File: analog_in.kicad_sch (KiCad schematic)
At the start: 5 parts, among them U18 INA600B

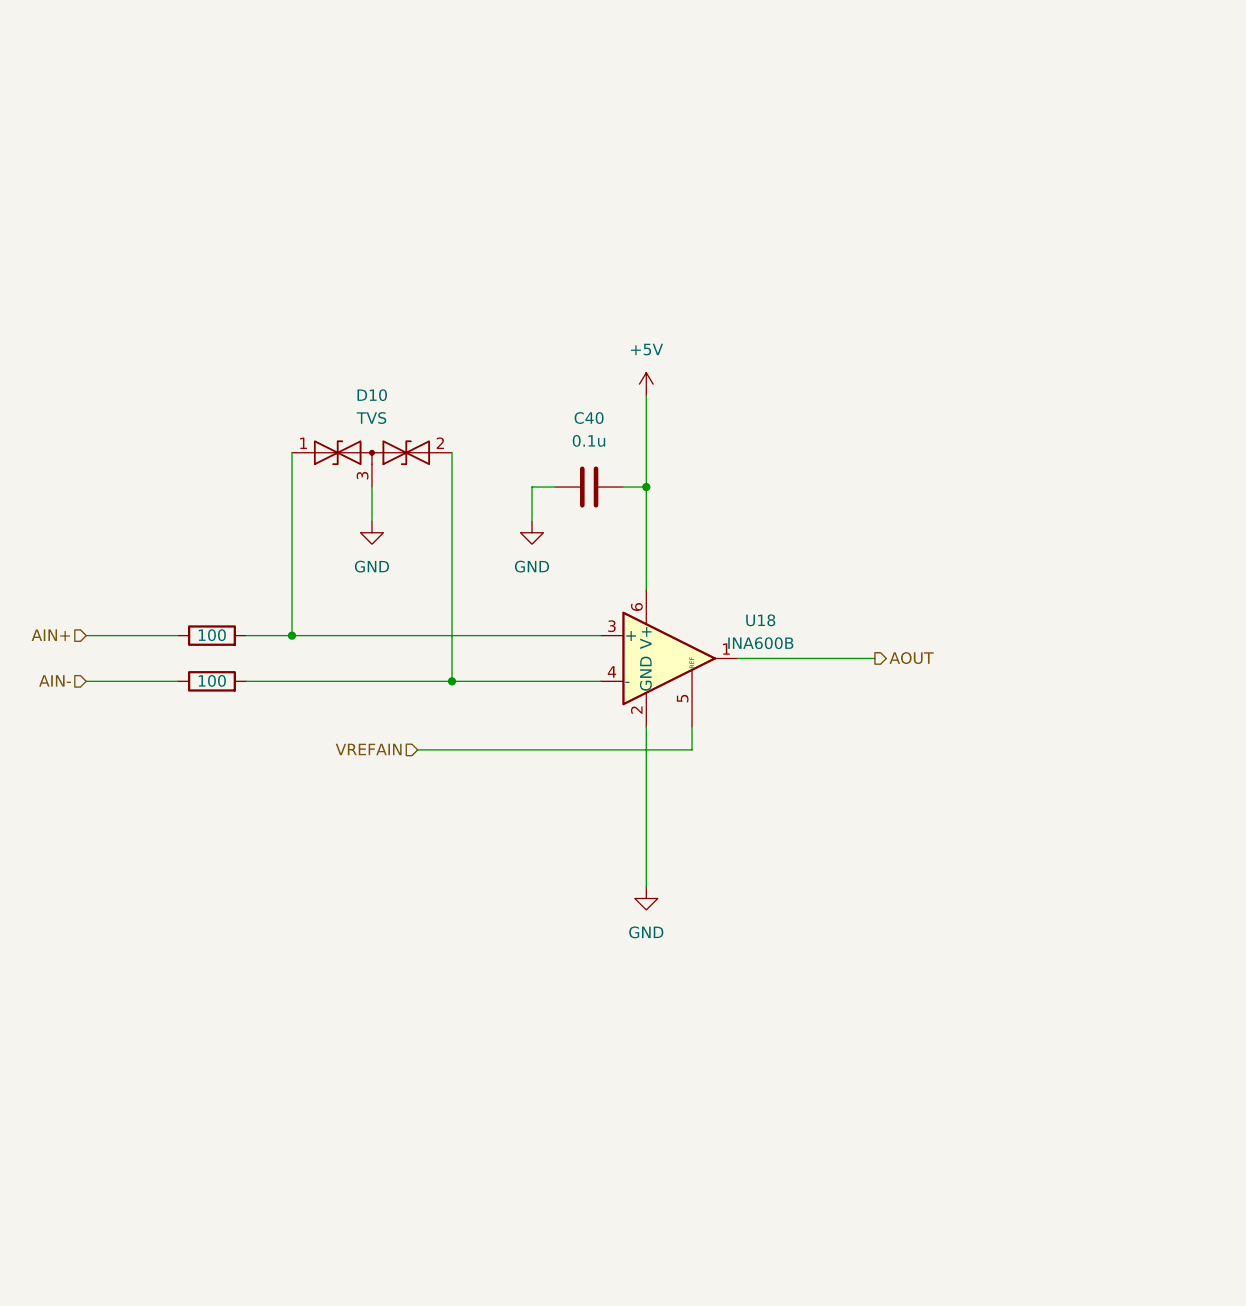
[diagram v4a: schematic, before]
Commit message: Adjusted components in I/O circuits
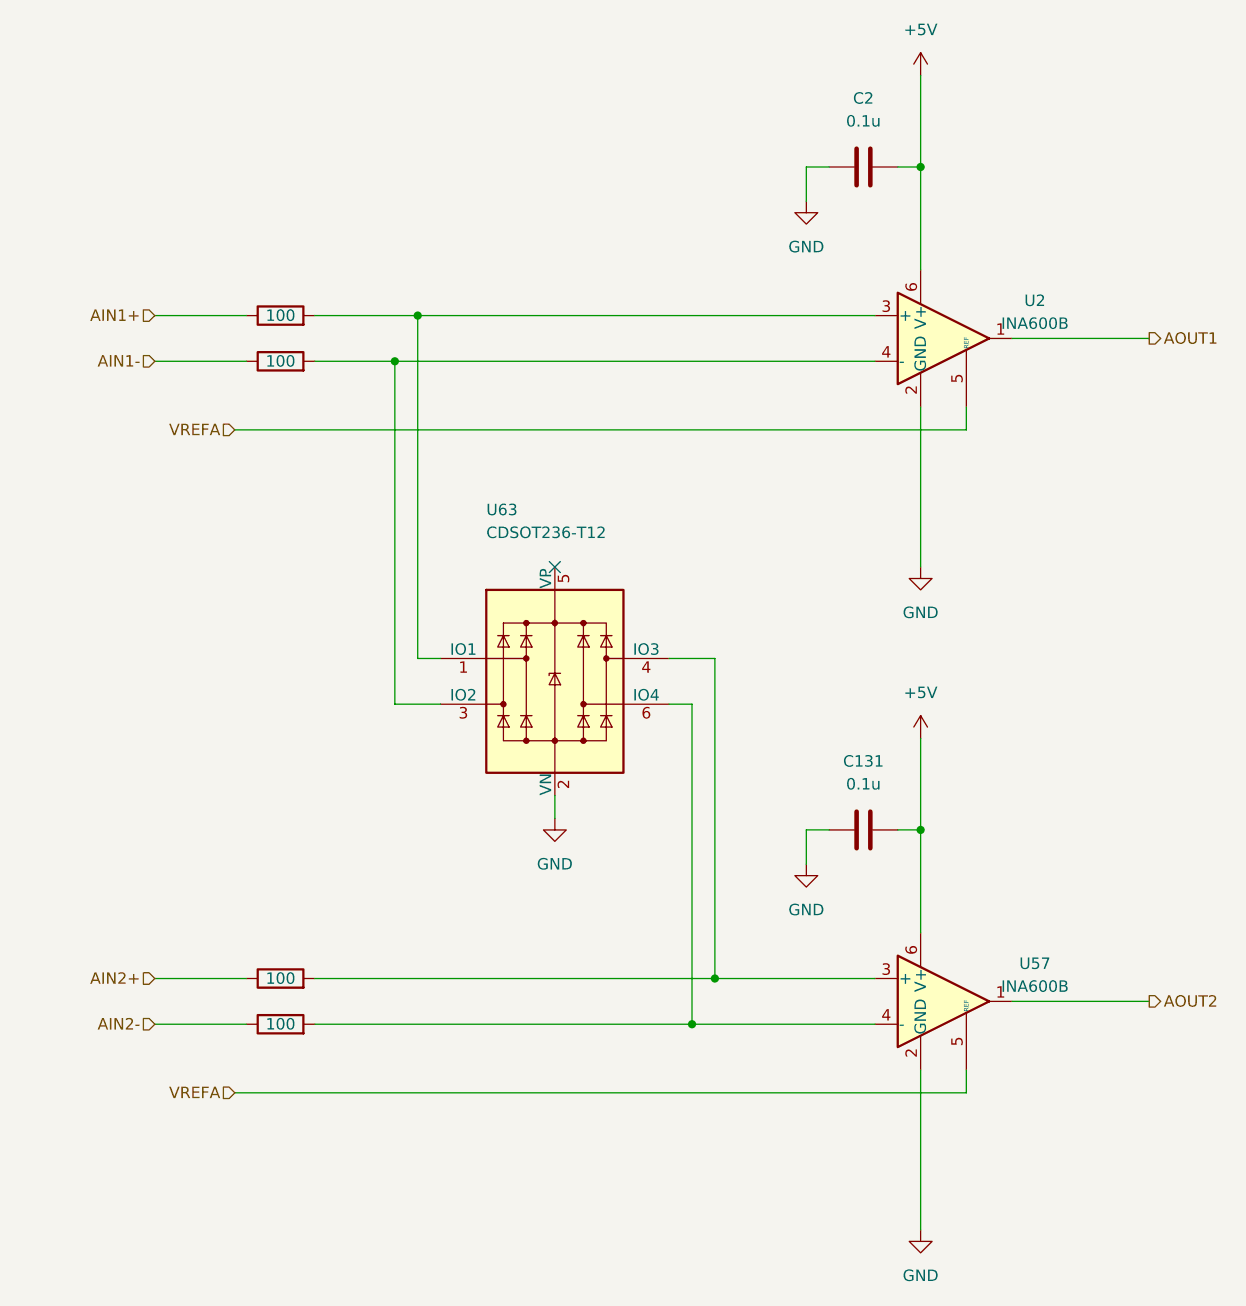
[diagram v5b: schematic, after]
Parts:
- removed C40: 0.1u, symbol Device:C
- removed D10: TVS, Package_TO_SOT_SMD:SOT-23, symbol Diode:SM712_SOT23
- removed R43, R44: 100, symbol Device:R
- removed U18: INA600B, Package_TO_SOT_SMD:SOT-23-6, symbol Amplifier_Current:INA181
- added C131, C2: 0.1u, symbol Device:C
- added R13, R14, R203, R204: 100, symbol Device:R
- added U2, U57: INA600B, Package_TO_SOT_SMD:SOT-23-6, symbol Amplifier_Current:INA181
- added U63: CDSOT236-T12, Package_TO_SOT_SMD:SOT-23-6, symbol Power_Protection:CDSOT236-0504C
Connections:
- net +5V: now also C131.2, C2.2, U2.6 (V+), U57.6 (V+)
- net GND: now also C131.1, C2.1, U2.2 (GND), U57.2 (GND), U63.2 (VN)
- new net: R13.2, U2.3 (+), U63.1 (IO1)
- new net: R14.2, U2.4 (-), U63.3 (IO2)
- new net: R203.2, U57.3 (+), U63.4 (IO3)
- new net: R204.2, U57.4 (-), U63.6 (IO4)
- new net AIN1+: R13.1
- new net AIN1-: R14.1
- new net AIN2+: R203.1
- new net AIN2-: R204.1
- new net AOUT1: U2.1
- new net AOUT2: U57.1
- new net VREFA: U2.5 (REF), U57.5 (REF)
- no-connect marks 0 -> 1

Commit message: Assigned proper footprints for all components
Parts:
- C131, C2: value 0.1u -> 100n; footprint (none) -> Capacitor_SMD:C_0603_1608Metric_Pad1.08x0.95mm_HandSolder
- R13, R14, R203, R204: footprint (none) -> Resistor_SMD:R_0603_1608Metric_Pad0.98x0.95mm_HandSolder
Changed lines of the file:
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@@
       (effects (font (size 1.27 1.27)))
     )
-    (property "Footprint" "" (at 124.46 58.928 90)
+    (property "Footprint" "Resistor_SMD:R_0603_1608Metric_Pad0.98x0.95mm_HandSolder" (at 124.46 58.928 90)
       (effects (font (size 1.27 1.27)) hide)
     )
@@
       (effects (font (size 1.27 1.27)))
     )
-    (property "Footprint" "" (at 124.46 132.588 90)
+    (property "Footprint" "Resistor_SMD:R_0603_1608Metric_Pad0.98x0.95mm_HandSolder" (at 124.46 132.588 90)
       (effects (font (size 1.27 1.27)) hide)
     )
@@
       (effects (font (size 1.27 1.27)))
     )
-    (property "Value" "0.1u" (at 189.23 109.22 90)
-      (effects (font (size 1.27 1.27)))
-    )
-    (property "Footprint" "" (at 193.04 113.3348 0)
+    (property "Value" "100n" (at 189.23 109.22 90)
+      (effects (font (size 1.27 1.27)))
+    )
+    (property "Footprint" "Capacitor_SMD:C_0603_1608Metric_Pad1.08x0.95mm_HandSolder" (at 193.04 113.3348 0)
       (effects (font (size 1.27 1.27)) hide)
     )
@@
       (effects (font (size 1.27 1.27)))
     )
-    (property "Value" "0.1u" (at 189.23 35.56 90)
-      (effects (font (size 1.27 1.27)))
-    )
-    (property "Footprint" "" (at 193.04 39.6748 0)
+    (property "Value" "100n" (at 189.23 35.56 90)
+      (effects (font (size 1.27 1.27)))
+    )
+    (property "Footprint" "Capacitor_SMD:C_0603_1608Metric_Pad1.08x0.95mm_HandSolder" (at 193.04 39.6748 0)
       (effects (font (size 1.27 1.27)) hide)
     )
@@
       (effects (font (size 1.27 1.27)))
     )
-    (property "Footprint" "" (at 124.46 64.008 90)
+    (property "Footprint" "Resistor_SMD:R_0603_1608Metric_Pad0.98x0.95mm_HandSolder" (at 124.46 64.008 90)
       (effects (font (size 1.27 1.27)) hide)
     )
@@
       (effects (font (size 1.27 1.27)))
     )
-    (property "Footprint" "" (at 124.46 137.668 90)
-      (effects (font (size 1.27 1.27)) hide)
-    )
+    (property "Footprint" "Resistor_SMD:R_0603_1608Metric_Pad0.98x0.95mm_HandSolder" (at 124.46 137.668 90)
+      (effects (font (size 1.27 1.27)) hide)
+    )

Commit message: Updated boards hierarchy
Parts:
- renumbered C131 to C3, R203 to R15, R204 to R16, U63 to U3, U57 to U8

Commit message: Finished annotation
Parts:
- renumbered C2 to C3301, C3 to C3302, R13 to R3301, R14 to R3302, R15 to R3303, R16 to R3304, U2 to U3301, U3 to U3302, U8 to U3303
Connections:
- net AOUT1 renamed AIN1
- net AOUT2 renamed AIN2
